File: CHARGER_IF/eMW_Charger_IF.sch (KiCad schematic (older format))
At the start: 15 parts, among them J1 CONN_01X02, J2 Booster_J1_J3, J3 Booster_J4_J2, J4 CONN_02X10, J5 CONN_02X10, U1 V7805-2000R, U2 Arduino-Socket, U3 SN74ACT08N, U4 SN74ACT08N

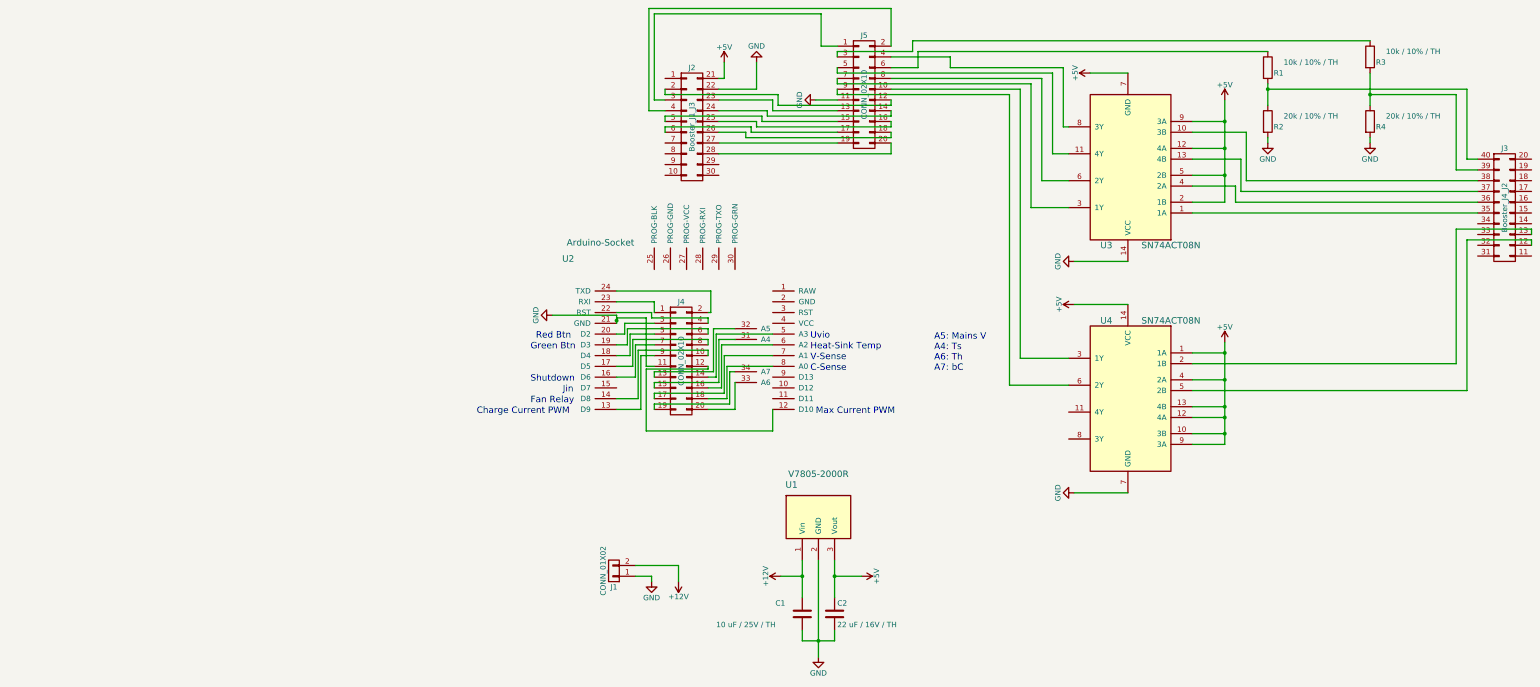
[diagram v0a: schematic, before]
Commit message: Charger IF
needs double checking and pin labels on silkscreen
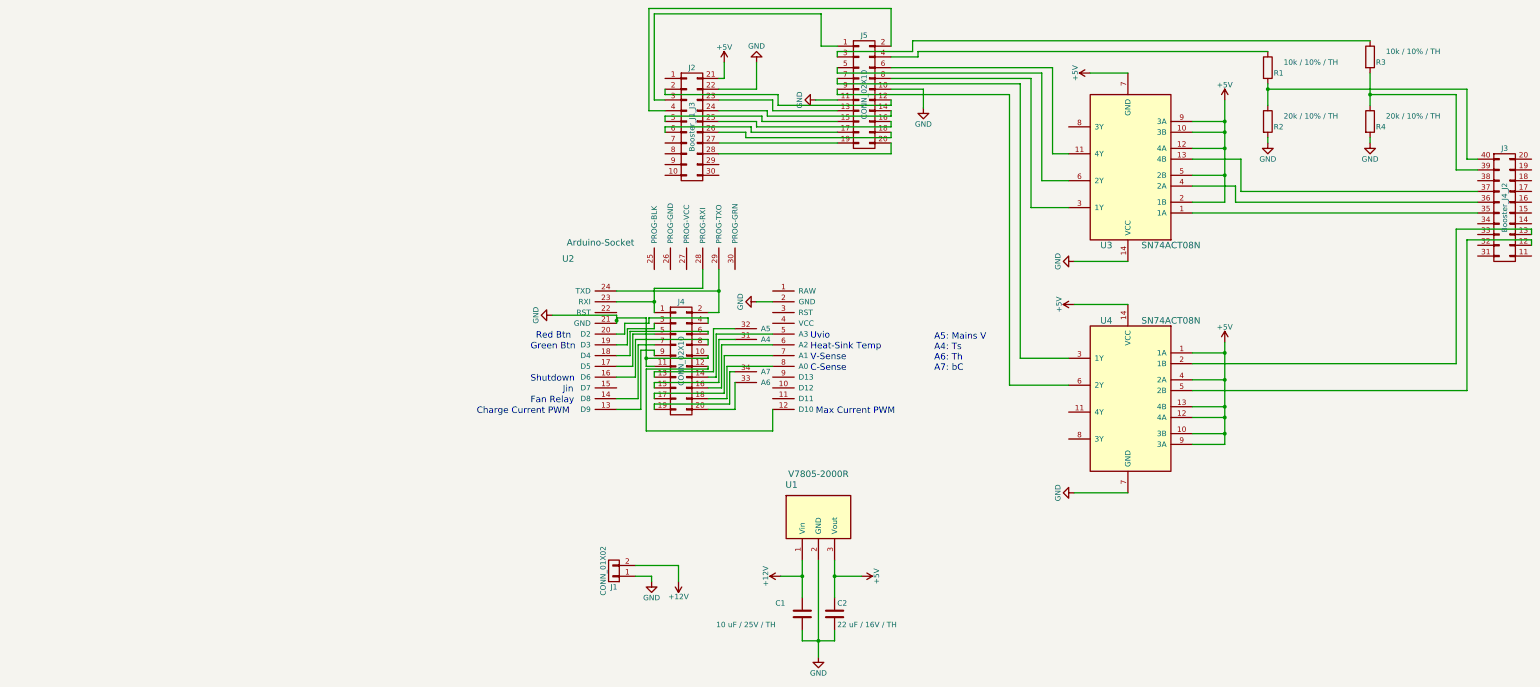
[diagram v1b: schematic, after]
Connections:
- net +5V: now also U3.10 (3B)
- net GND: now also J4.10 (P10), J5.10 (P10), U2.2 (GND)
- net at J3.38 (P38): no longer U3.10 (3B)
- net at U3.11 (4Y): now also J5.6 (P6); no longer J5.5 (P5)
- net at U3.3 (1Y): now also J5.8 (P8); no longer J5.7 (P7)
- net at U3.6 (2Y): now also J5.5 (P5); no longer J5.8 (P8)
- net at U3.8 (3Y): no longer J5.4 (P4)
- net at U4.3 (1Y): now also J5.7 (P7); no longer J5.10 (P10)
- net at R1.1: now also J5.4 (P4); no longer J5.6 (P6)
- net at U2.14 (D8): now also J4.7 (P7); no longer J4.10 (P10)
- net at U2.16 (D6): now also J4.8 (P8); no longer J4.7 (P7)
- net at U2.17 (D5): now also J4.5 (P5); no longer J4.8 (P8)
- net at U2.18 (D4): now also J4.6 (P6); no longer J4.5 (P5)
- net at U2.19 (D3): now also J4.3 (P3); no longer J4.6 (P6)
- net at U2.20 (D2): now also J4.4 (P4); no longer J4.3 (P3)
- net at U2.22 (RST): no longer J4.4 (P4)
- net at J4.1 (P1), U2.23 (RXI): now also U2.28 (PROG-RXI)
- net at J4.2 (P2), U2.24 (TXD): now also U2.29 (PROG-TXO)
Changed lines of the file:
@@
 $EndComp
 Wire Wire Line
-	6300 2100 6250 2100
-Wire Wire Line
-	6250 2100 6250 1550
-Wire Wire Line
-	6250 1550 5200 1550
-Wire Wire Line
-	6150 1700 6150 1700
-Wire Wire Line
-	6150 1600 6150 2350
+	6150 1550 6150 2350
 Wire Wire Line
 	6150 2350 6300 2350
@@
 	6050 2600 6300 2600
 Wire Wire Line
-	6050 1650 6050 2600
-Wire Wire Line
 	5950 2850 6300 2850
 Wire Wire Line
-	5950 1700 5950 2850
-Wire Wire Line
-	5850 1750 5850 4250
+	5950 1650 5950 2850
+Wire Wire Line
+	5850 1700 5850 4250
 Wire Wire Line
 	5850 4250 6300 4250
@@
 	9900 1800 9100 1800
 Wire Wire Line
-	7450 2150 7950 2150
-Wire Wire Line
-	7950 2150 7950 2600
-Wire Wire Line
-	7950 2600 10100 2600
-Wire Wire Line
 	7450 2400 7900 2400
 Wire Wire Line
@@
 	2675 6175 2675 6325
 Wire Wire Line
-	2100 3625 2975 3625
-Wire Wire Line
-	2975 3625 2975 3825
-Wire Wire Line
-	2975 3825 2950 3825
-Wire Wire Line
-	2100 3725 2450 3725
-Wire Wire Line
-	2450 3725 2450 3825
-Wire Wire Line
-	2100 3825 2425 3825
-Wire Wire Line
-	2425 3825 2425 3875
-Wire Wire Line
-	2425 3875 2950 3875
-Wire Wire Line
-	2950 3875 2950 3925
-Wire Wire Line
 	2100 4025 2175 4025
 Wire Wire Line
 	2175 4025 2175 3925
 Wire Wire Line
-	2175 3925 2450 3925
-Wire Wire Line
 	2100 4125 2200 4125
 Wire Wire Line
 	2200 4125 2200 3975
 Wire Wire Line
-	2200 3975 2950 3975
-Wire Wire Line
-	2950 3975 2950 4025
-Wire Wire Line
 	3550 4725 3550 4925
 Wire Wire Line
@@
 	3200 4725 3200 4475
 Wire Wire Line
-	2100 4225 2225 4225
-Wire Wire Line
-	2225 4225 2225 4025
-Wire Wire Line
-	2225 4025 2450 4025
-Wire Wire Line
-	2100 4325 2250 4325
-Wire Wire Line
-	2250 4325 2250 4075
-Wire Wire Line
-	2250 4075 2950 4075
-Wire Wire Line
-	2950 4075 2950 4125
-Wire Wire Line
-	2100 4425 2275 4425
-Wire Wire Line
-	2275 4425 2275 4125
-Wire Wire Line
-	2275 4125 2450 4125
-Wire Wire Line
-	2100 4625 2300 4625
-Wire Wire Line
-	2300 4625 2300 4175
-Wire Wire Line
-	2300 4175 2950 4175
-Wire Wire Line
-	2950 4175 2950 4225
-Wire Wire Line
-	2100 4725 2325 4725
-Wire Wire Line
-	2325 4725 2325 4225
-Wire Wire Line
-	2325 4225 2450 4225
+	2225 4225 2100 4225
+Wire Wire Line
+	2225 4000 2225 4225
+Wire Wire Line
+	2250 4325 2100 4325
+Wire Wire Line
+	2250 4025 2250 4325
+Wire Wire Line
+	2275 4425 2100 4425
+Wire Wire Line
+	2275 4075 2275 4425
+Wire Wire Line
+	2300 4625 2100 4625
+Wire Wire Line
+	2300 4125 2300 4625
+Wire Wire Line
+	2325 4725 2100 4725
+Wire Wire Line
+	2325 4175 2325 4725
 Wire Wire Line
 	2375 4925 2375 4350
@@
 	2950 4350 2950 4325
 Wire Wire Line
-	2450 4325 2375 4325
-Wire Wire Line
-	2375 4325 2375 3875
+	2375 4325 2450 4325
+Wire Wire Line
+	2375 3875 2375 4325
 Wire Wire Line
 	2375 3875 2100 3875
@@
 Wire Wire Line
 	3950 1850 4150 1850
-Wire Wire Line
-	4650 1550 4900 1550
-Wire Wire Line
-	5750 1800 4150 1800
-Wire Wire Line
-	4150 1800 4150 1750
-Wire Wire Line
-	5850 1750 4650 1750
-Wire Wire Line
-	5950 1700 4150 1700
-Wire Wire Line
-	4150 1700 4150 1650
-Wire Wire Line
-	6050 1650 4650 1650
-Wire Wire Line
-	6150 1600 4150 1600
-Wire Wire Line
-	4150 1600 4150 1550
-Wire Wire Line
-	5200 1550 5200 1450
-Wire Wire Line
-	5200 1450 4650 1450
-Wire Wire Line
-	4900 1550 4900 1400
 Wire Wire Line
 	4900 1400 8150 1400
@@
 Wire Wire Line
 	10600 3050 10600 3100
+$Comp
+L GND #PWR018
+U 1 1 597EC399
+P 3400 3725
+F 0 "#PWR018" H 3400 3475 50  0001 C CNN
+F 1 "GND" H 3400 3575 50  0000 C CNN
+F 2 "" H 3400 3725 50  0001 C CNN
+F 3 "" H 3400 3725 50  0001 C CNN
+	1    3400 3725
+	0    1    1    0
+$EndComp
+Wire Wire Line
+	3400 3725 3550 3725
+Wire Wire Line
+	3050 3825 2950 3825
+Wire Wire Line
+	3050 3425 3050 3825
+Wire Wire Line
+	2450 3600 2450 3825
+Wire Wire Line
+	2450 3600 2900 3600
+Wire Wire Line
+	2900 3600 2900 3425
+Wire Wire Line
+	3050 3625 2100 3625
+Connection ~ 3050 3625
+Wire Wire Line
+	2100 3725 2450 3725
+Connection ~ 2450 3725
+Wire Wire Line
+	7450 2150 7750 2150
+Connection ~ 7750 2150
+Wire Wire Line
+	2175 3925 2400 3925
+Wire Wire Line
+	2400 3925 2400 3875
+Wire Wire Line
+	2400 3875 2950 3875
+Wire Wire Line
+	2950 3875 2950 3925
+Wire Wire Line
+	2200 3975 2450 3975
+Wire Wire Line
+	2450 3975 2450 3925
+Wire Wire Line
+	2225 4000 2950 4000
+Wire Wire Line
+	2950 4000 2950 4025
+Wire Wire Line
+	2250 4025 2450 4025
+Wire Wire Line
+	2275 4075 2950 4075
+Wire Wire Line
+	2950 4075 2950 4125
+Wire Wire Line
+	2300 4125 2450 4125
+Wire Wire Line
+	2325 4175 2450 4175
+Wire Wire Line
+	2450 4175 2450 4225
+Wire Wire Line
+	2375 4250 2950 4250
+Wire Wire Line
+	2950 4250 2950 4225
+Connection ~ 2375 4250
+Wire Wire Line
+	4900 1400 4900 1450
+Wire Wire Line
+	4900 1450 4650 1450
+Wire Wire Line
+	4650 1550 6150 1550
+Wire Wire Line
+	4150 1550 4150 1600
+Wire Wire Line
+	4150 1600 6050 1600
+Wire Wire Line
+	6050 1600 6050 2600
+Wire Wire Line
+	4650 1650 5950 1650
+Wire Wire Line
+	5850 1700 4150 1700
+Wire Wire Line
+	4150 1700 4150 1650
+Wire Wire Line
+	5750 1800 4150 1800
+Wire Wire Line
+	4150 1800 4150 1750
+$Comp
+L GND #PWR019
+U 1 1 597F0299
+P 4950 1925
+F 0 "#PWR019" H 4950 1675 50  0001 C CNN
+F 1 "GND" H 4950 1775 50  0000 C CNN
+F 2 "" H 4950 1925 50  0000 C CNN
+F 3 "" H 4950 1925 50  0000 C CNN
+	1    4950 1925
+	1    0    0    -1
+$EndComp
+Wire Wire Line
+	4950 1925 4950 1750
+Wire Wire Line
+	4950 1750 4650 1750
 $EndSCHEMATC

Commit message: Final Charger IF
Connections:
- net +5V: no longer U3.10 (3B)
- net at U3.8 (3Y): now also J5.12 (P12)
- net at J2.2 (P2): no longer J5.12 (P12)
- net at J3.38 (P38): now also U3.10 (3B)
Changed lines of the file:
@@
 	3550 1950 4150 1950
-Wire Wire Line
-	2550 1750 2550 1800
-Wire Wire Line
-	2550 1800 3600 1800
-Wire Wire Line
-	3600 1800 3600 1900
-Wire Wire Line
-	3600 1900 4650 1900
-Wire Wire Line
-	4650 1900 4650 1850
 Wire Wire Line
 	3950 1850 4150 1850
@@
 	2100 3725 2450 3725
 Connection ~ 2450 3725
-Wire Wire Line
-	7450 2150 7750 2150
-Connection ~ 7750 2150
 Wire Wire Line
 	2175 3925 2400 3925
@@
 Wire Wire Line
 	4950 1750 4650 1750
+Wire Wire Line
+	4650 1850 6300 1850
+Wire Wire Line
+	6300 1850 6300 2100
+Wire Wire Line
+	7450 2150 8000 2150
+Wire Wire Line
+	8000 2150 8000 2600
+Wire Wire Line
+	8000 2600 10100 2600
 $EndSCHEMATC

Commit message: Finals w/ pdf
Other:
- note added: "rLoop Charger IF Board"
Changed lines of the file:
@@
 Wire Wire Line
 	8000 2600 10100 2600
+Text Notes 7225 6925 0    157  ~ 0
+rLoop Charger IF Board
 $EndSCHEMATC

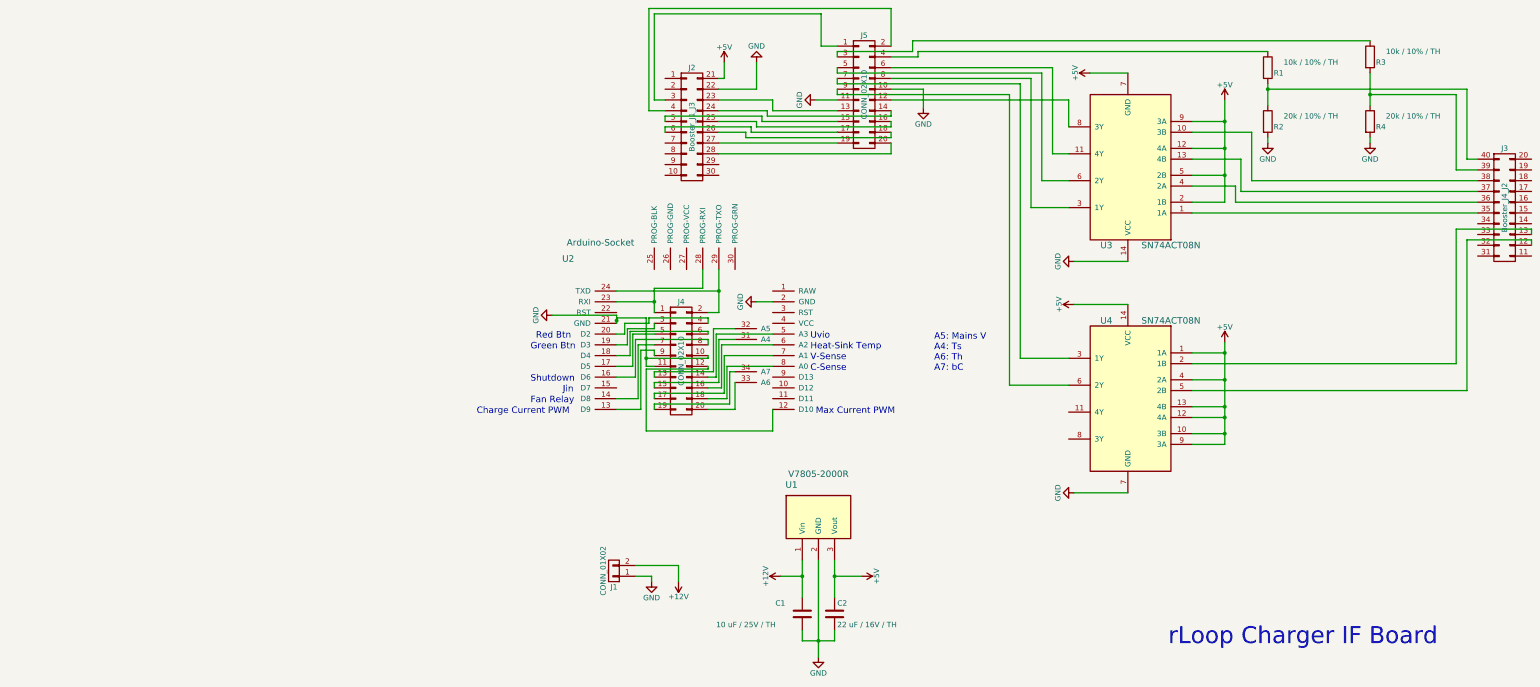
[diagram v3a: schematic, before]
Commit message: Cleaned up PN for BOM
need exact PN for excel sheet on one or two items.
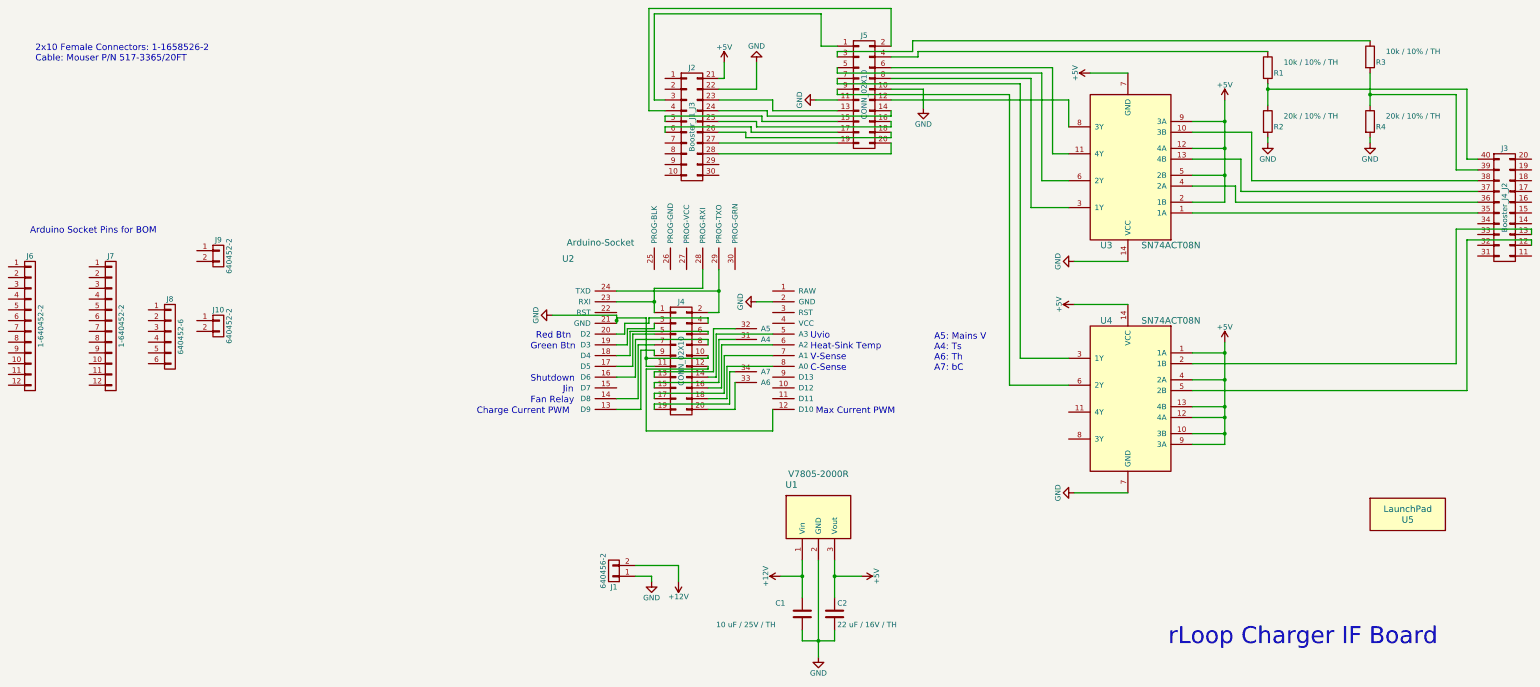
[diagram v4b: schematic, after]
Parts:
- added J10, J9: 640452-2, symbol CONN_01X02
- added J6, J7: 1-640452-2, symbol CONN_01X12
- added J8: 640452-6, symbol CONN_01X06
- added U5: LaunchPad, symbol LaunchPad
- C1: Mouser P/N (none) -> 810-FG26X7R1E106KRT6; Mouser PN 810-FG26X7R1E106KRT6 -> (none)
- C2: Mouser P/N (none) -> 810-FG22X7R1E226MRT6; Mouser PN 810-FG22X7R1E226MRT6 -> (none)
- J1: value CONN_01X02 -> 640456-2; Mouser P/N (none) -> 571-6404562; Mouser URL (none) -> http://www.mouser.com/search/ProductDetail.aspx?R=0virtualk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
- J2, J3: Mouser P/N (none) -> 571-6-534206-0; Mouser URL (none) -> http://www.mouser.com/search/ProductDetail.aspx?R=0virtualk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
- J4, J5: Mouser P/N (none) -> 571-2-1761603-7; Mouser URL (none) -> http://www.mouser.com/search/ProductDetail.aspx?R=0virtualk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
- R1, R3: Mouser P/N (none) -> 71-CCF0710K0JKE36; Mouser URL (none) -> http://www.mouser.com/search/ProductDetail.aspx?R=0virtualk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
- R2, R4: Mouser P/N (none) -> 71-CCF0720K0JKE36; Mouser URL (none) -> http://www.mouser.com/search/ProductDetail.aspx?R=0virtualk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
- U1: Mouser P/N (none) -> 490-V7805-2000R; Mouser PN 490-V7805-2000R -> (none)
- U3, U4: Mouser P/N (none) -> 595-SN74ACT08N; Mouser PN 595-SN74ACT08N -> (none)
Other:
- note added: "2x10 Female Connectors: 1-1658526-2\nCable: Mouser P/N 517-3365/20FT"
- note added: "Arduino Socket Pins for BOM"
